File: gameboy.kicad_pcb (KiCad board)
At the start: 4 copper layers, 90 x 125 mm, 102 parts, among them J1 SM03B-SRSS-TB, J2 FPC-05F-12PH20, J3 Conn_01x02, J4 Conn_01x02, J5 Conn_01x02, J6 SD_Card_Receptacle, J7 USB_C_Receptacle_USB2.0_16P, Q1 SS8050, Q2 AO3401A, Q3 SS8050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

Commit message: mcu layout
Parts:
- moved C26 198.6 mm to (226.2, 131.5)
- moved R21 196.0 mm to (226.2, 133.5), turned to 180 degrees
- moved R22 195.7 mm to (226.2, 135.5), turned to 180 degrees
- moved R20 194.7 mm to (225.9, 129.0), turned to 90 degrees
- moved C25 191.1 mm to (217.9, 128.8), turned to 90 degrees
- moved L2 184.5 mm to (220.0, 134.5), turned to 180 degrees
- moved C23 182.7 mm to (202.1, 134.5), turned to 90 degrees
- moved R19 179.6 mm to (204.0, 134.5), turned to 90 degrees
- moved R18 177.7 mm to (198.1, 137.5)
- moved C24 176.4 mm to (201.1, 126.5), turned to 90 degrees
- moved U7 172.1 mm to (221.9, 129.0)
- moved R16 171.0 mm to (199.1, 126.5), turned to -90 degrees
- moved R17 168.1 mm to (197.1, 126.5), turned to -90 degrees
- moved SW8 166.3 mm to (154.7, 174.0), turned to -90 degrees
- moved Q2 164.8 mm to (202.9, 130.5), turned to 180 degrees
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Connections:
- net +5V renamed VDC
- C26 pad 1: +3.3V -> +3V3
- L2 pad 2: +3.3V -> +3V3
- R20 pad 1: +3.3V -> +3V3
- R21 pad 1: +3.3V -> +3V3
- U7 pad 6: +3.3V -> +3V3
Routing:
- net GND: track 0.00 -> 143.2 mm, vias 0 -> 34
- net /Power/USB_VBUS: track 0.00 -> 55.5 mm
- net +3V3: track 0.00 -> 49.0 mm, vias 0 -> 7
- net Net-(J6-DAT2): track 0.00 -> 15.4 mm
- net /MCU/SD_SS: track 0.00 -> 13.5 mm
- net /MCU/SD_MOSI: track 0.00 -> 11.6 mm
- net /Buttons/BTN_RIGHT: track 0.00 -> 10.0 mm
- net VDC: track 0.00 -> 10.00 mm
- net /Buttons/BTN_B: track 0.00 -> 9.92 mm
- net /Buttons/BTN_UP: track 0.00 -> 9.82 mm
- net /Buttons/BTN_LEFT: track 0.00 -> 9.82 mm
- net /Buttons/BTN_DOWN: track 0.00 -> 9.82 mm
- net /Buttons/BTN_A: track 0.00 -> 9.73 mm
- net +1V1: track 0.00 -> 9.15 mm
- net Net-(J7-CC1): track 0.00 -> 8.73 mm
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- added copper zone on F.Cu, net +1V1
- added copper zone on B.Cu, net +3V3
- added copper zone on F.Cu, net +3V3
- added copper zone on F.Cu, net GND
- added copper zone on In1.Cu, net GND
- added copper zone on In2.Cu, net GND
- added copper zone on F.Cu, net Net-(U1-VREG_LX)
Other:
- board size 90 x 125 mm -> 177.4 x 125 mm

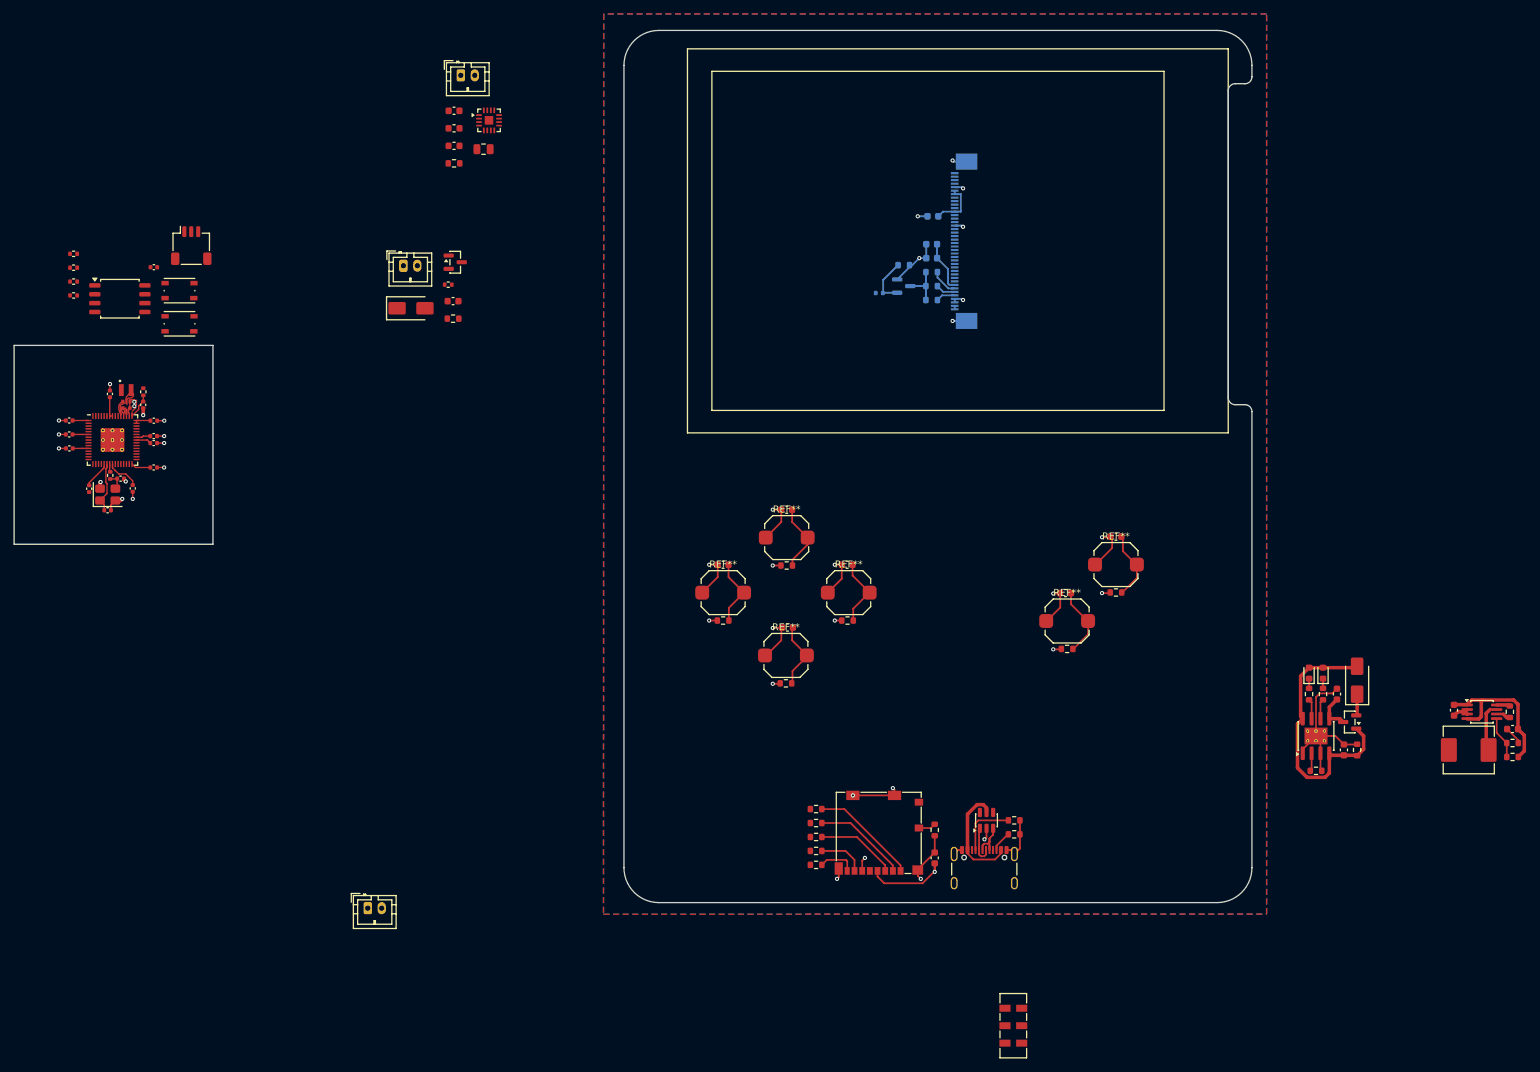
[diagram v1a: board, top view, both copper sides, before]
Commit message: place mcu on board
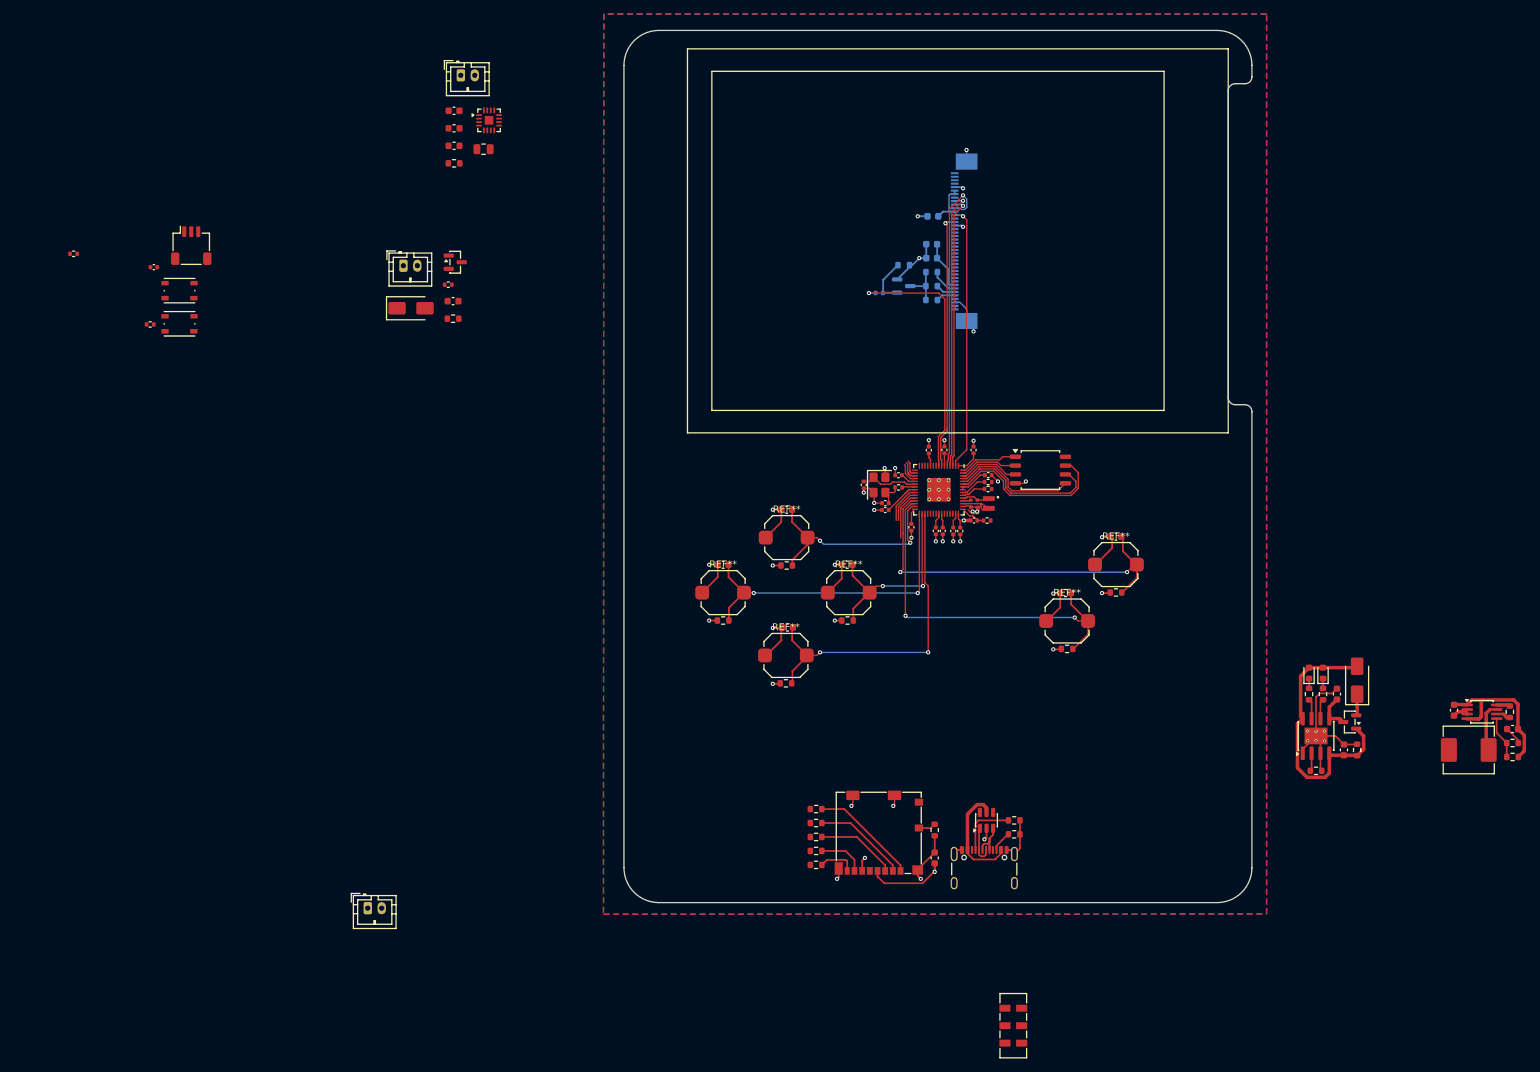
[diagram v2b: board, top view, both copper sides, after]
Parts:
- added C31: 100n, Capacitor_SMD:C_0402_1005Metric, F.Cu at (146.1, 103.1)
- moved R4 134.6 mm to (151.1, 96.1), turned to 180 degrees
- moved R5 134.4 mm to (151.1, 97.1), turned to 180 degrees
- moved U2 134.2 mm to (158.6, 94.4)
- moved C9 129.7 mm to (149.0, 91.5), turned to 90 degrees
- moved C14 126.4 mm to (151.1, 95.1), turned to 0 degrees
- moved C8 125.5 mm to (144.8, 91.5), turned to 90 degrees
- moved L1 124.7 mm to (151.2, 99.2), turned to -90 degrees
- moved C11 123.2 mm to (142.6, 91.5), turned to 90 degrees
- moved C4 122.8 mm to (149.5, 99.2), turned to -90 degrees
- moved R1 122.3 mm to (150.9, 101.6), turned to 180 degrees
- moved C1 121.8 mm to (148.6, 99.2), turned to -90 degrees
- moved C6 120.2 mm to (149.1, 101.6), turned to 180 degrees
- moved U1 118.6 mm to (144.0, 97.2), turned to -90 degrees
- moved C13 116.7 mm to (147.1, 103.1), turned to -90 degrees
- moved C15 116.0 mm to (138.2, 95.1), turned to 180 degrees
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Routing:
- net /Buttons/BTN_A: track 9.73 -> 55.5 mm, vias 0 -> 2
- net /LCD/LCD_DC: track 0.00 -> 43.6 mm, vias 0 -> 1
- net /Buttons/BTN_B: track 9.92 -> 53.3 mm, vias 0 -> 2
- net /LCD/LCD_CS: track 0.00 -> 40.0 mm, vias 0 -> 1
- net /LCD/LCD_SCL: track 0.00 -> 39.1 mm, vias 0 -> 1
- net /LCD/LCD_SDA: track 0.00 -> 37.9 mm, vias 0 -> 1
- net /Buttons/BTN_DOWN: track 9.82 -> 47.5 mm, vias 0 -> 2
- net /LCD/LCD_RST: track 0.00 -> 36.7 mm, vias 0 -> 1
- net /LCD/LCD_BL: track 0.00 -> 36.5 mm, vias 0 -> 1
- net /Buttons/BTN_LEFT: track 9.82 -> 46.2 mm, vias 0 -> 2
- net /MCU/QSPI_SD3: track 0.00 -> 24.7 mm
- net /MCU/QSPI_SCLK: track 0.00 -> 22.1 mm
- net /Buttons/BTN_UP: track 9.82 -> 31.1 mm, vias 0 -> 2
- net /Buttons/BTN_RIGHT: track 10.0 -> 28.5 mm, vias 0 -> 2
- net /MCU/QSPI_SD0: track 0.00 -> 18.0 mm
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- removed copper zone on F.Cu, net +1V1
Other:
- board size 177.4 x 125 mm -> 90 x 125 mm

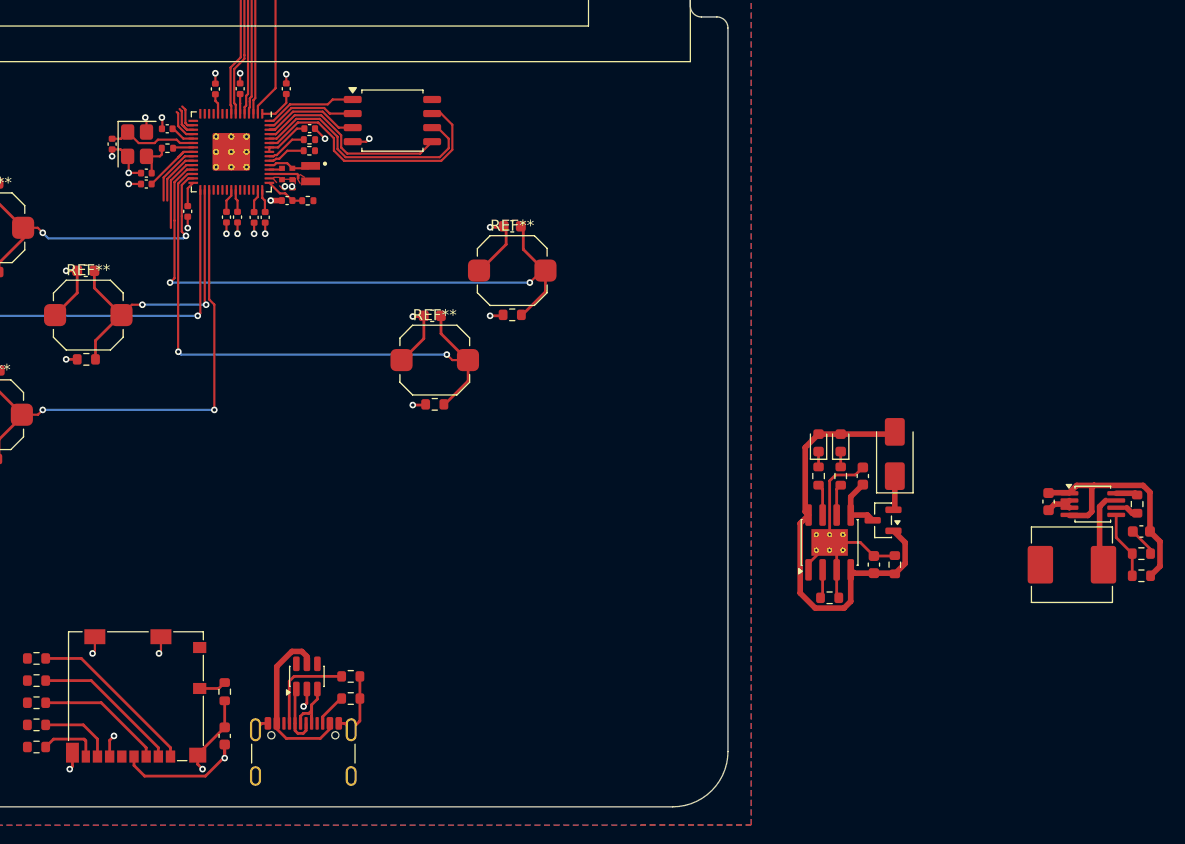
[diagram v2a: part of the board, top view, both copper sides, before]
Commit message: add partial power system
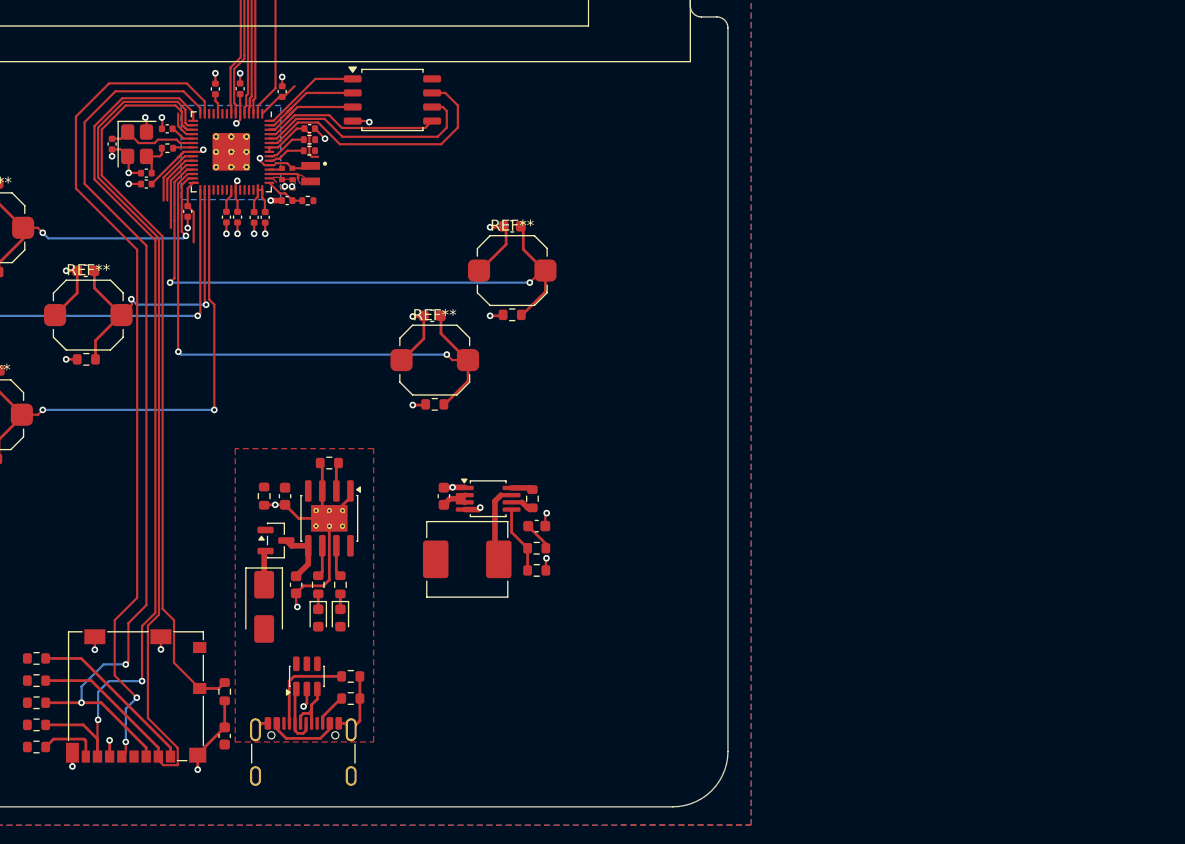
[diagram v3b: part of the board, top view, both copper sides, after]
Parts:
- moved D3 58.6 mm to (147.0, 138.3), turned to -90 degrees
- moved R19 57.3 mm to (147.0, 128.3), turned to -90 degrees
- moved Q2 54.9 mm to (148.1, 132.3), turned to 0 degrees
- moved C25 54.6 mm to (163.2, 128.3)
- moved C26 54.6 mm to (171.6, 131.0)
- moved L2 54.6 mm to (165.3, 134.0)
- moved R20 54.6 mm to (171.2, 128.5)
- moved R21 54.6 mm to (171.6, 133.0)
- moved R22 54.6 mm to (171.6, 135.0)
- moved U7 54.6 mm to (167.2, 128.5)
- moved C23 53.6 mm to (148.9, 128.3), turned to -90 degrees
- moved C24 52.1 mm to (149.9, 136.3), turned to -90 degrees
- moved D1 49.8 mm to (151.9, 139.3), turned to -90 degrees
- moved R16 48.2 mm to (151.9, 136.3), turned to 90 degrees
- moved R18 46.8 mm to (152.9, 125.3), turned to 180 degrees
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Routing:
- net /MCU/SD_CLK: track 0.00 -> 77.0 mm, vias 0 -> 2
- net /MCU/SD_MISO: track 6.79 -> 81.2 mm, vias 0 -> 2
- net /MCU/SD_SS: track 15.9 -> 88.3 mm
- net /MCU/SD_MOSI: track 11.6 -> 83.0 mm, vias 0 -> 2
- net /MCU/SD_DET: track 5.75 -> 68.0 mm
- net /Power/USB_VBUS: track 55.5 -> 7.30 mm
- net GND: track 147.5 -> 129.9 mm, vias 36 -> 42
- net +1V1: track 13.6 -> 17.7 mm, vias 0 -> 4
- net +3V3: track 52.5 -> 48.9 mm, vias 7 -> 6
- net /MCU/QSPI_SD0: track 18.0 -> 16.2 mm
- net /MCU/QSPI_SCLK: track 22.1 -> 20.8 mm
- net /MCU/QSPI_SD1: track 8.39 -> 9.27 mm
- net /Buttons/BTN_RIGHT: track 28.5 -> 29.3 mm
- net /MCU/QSPI_SS: track 8.33 -> 9.10 mm
- added copper zone on B.Cu, net +1V1
- added copper zone on F.Cu, net /Power/USB_VBUS

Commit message: more routing
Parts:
- added SW8: SW_Slide_DPDT, Button_Switch_SMD:SW_DPDT_CK_JS202011JCQN, F.Cu at (88.0, 86.2)
- J3, J4, J5: footprint Connector_JST:JST_PH_B2B-PH-K_1x02_P2.00mm_Vertical -> Connector_JST:JST_PH_S2B-PH-SM4-TB_1x02-1MP_P2.00mm_Horizontal; moved to B.Cu
- moved SW8 103.0 mm to (103.8, 84.5)
- moved J3 101.8 mm to (132.5, 83.5), turned to 180 degrees
- moved J4 65.9 mm to (123.0, 83.5), turned to 180 degrees
- moved J5 49.7 mm to (113.5, 83.5), turned to 180 degrees
- moved C25 4.48 mm to (159.9, 131.3)
- moved R20 4.48 mm to (167.9, 131.5)
- moved U7 4.48 mm to (163.9, 131.5)
- moved C26 4.48 mm to (168.3, 134.0)
- moved L2 4.48 mm to (162.0, 137.0)
- moved R21 4.48 mm to (168.3, 136.0)
- moved R22 4.48 mm to (168.3, 138.0)
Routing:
- net VDC: track 10.00 -> 234.9 mm, vias 0 -> 12
- net Net-(D3-K): track 3.09 -> 98.9 mm, vias 0 -> 6
- net /Power/BAT+: track 5.39 -> 88.4 mm, vias 0 -> 10
- net /MCU/USB_D-: track 0.00 -> 78.8 mm
- net /MCU/USB_D+: track 0.00 -> 78.1 mm
- net GND: track 129.9 -> 134.3 mm, vias 42 -> 44
- added copper zone on B.Cu, net /Power/BAT+
- added copper zone on F.Cu, net /Power/BAT+
- added copper zone on B.Cu, net Net-(D3-K)
- added copper zone on F.Cu, net Net-(D3-K)
- added copper zone on B.Cu, net VDC
- added copper zone on F.Cu, net VDC

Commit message: route vibration and speaker
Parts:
- removed the SW8 at (103.8, 84.5)
- C27, C29, C30, D4, FB1, FB2, Q3, R26, R28, U5: moved to B.Cu
- R27: footprint Resistor_SMD:R_0402_1005Metric -> Resistor_SMD:R_0603_1608Metric; moved to B.Cu
- moved J1 153.9 mm to (161.5, 152.5)
- moved D4 93.1 mm to (161.1, 80.0), turned to 90 degrees
- moved C27 89.7 mm to (163.6, 80.0), turned to 90 degrees
- moved R26 88.1 mm to (162.4, 44.0), turned to 90 degrees
- moved R27 85.6 mm to (157.8, 84.2), turned to 90 degrees
- moved C29 85.1 mm to (159.6, 45.3), turned to 180 degrees
- moved Q3 83.9 mm to (157.3, 79.5)
- moved R28 83.0 mm to (156.9, 82.0), turned to 180 degrees
- moved FB2 82.7 mm to (156.9, 39.6), turned to 180 degrees
- moved FB1 82.4 mm to (156.9, 41.3), turned to 180 degrees
- moved U5 81.6 mm to (161.1, 40.3), turned to 180 degrees
- moved C30 81.0 mm to (159.6, 43.6), turned to 180 degrees
- moved J3 72.1 mm to (61.2, 94.5)
- moved J4 49.6 mm to (150.3, 42.1), turned to 90 degrees
- moved J5 36.8 mm to (150.2, 80.8), turned to 90 degrees
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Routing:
- net /Audio/I2S_LRCLK: track 0.00 -> 84.2 mm, vias 0 -> 1
- net /Audio/I2S_BCLK: track 0.00 -> 78.8 mm, vias 0 -> 1
- net /Audio/I2S_DIN: track 0.00 -> 76.4 mm, vias 0 -> 1
- net /Audio/I2S_SDMODE: track 0.00 -> 71.4 mm, vias 0 -> 1
- net /MCU/SWD: track 4.98 -> 74.8 mm, vias 0 -> 2
- net /MCU/SWCLK: track 5.55 -> 74.7 mm, vias 0 -> 2
- net /MCU/VIB_EN: track 2.80 -> 26.9 mm, vias 0 -> 1
- net /MCU/USB_D+: track 78.1 -> 54.1 mm
- net /MCU/USB_D-: track 78.8 -> 55.7 mm
- net Net-(D4-A): track 0.00 -> 11.8 mm
- net Net-(D3-K): track 98.9 -> 105.8 mm
- net /Power/BAT+: track 88.4 -> 83.5 mm, vias 10 -> 7
- net GND: track 134.3 -> 138.6 mm, vias 44 -> 51
- net VDC: track 234.9 -> 239.0 mm, vias 12 -> 9
- net Net-(J4-Pin_1): track 0.00 -> 3.69 mm
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- added copper zone on B.Cu, net GND
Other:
- board text removed: "LCD"
